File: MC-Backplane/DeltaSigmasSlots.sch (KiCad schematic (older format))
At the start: 2 parts, among them J21 86094328314755V1LF, J22 86094328314755V1LF

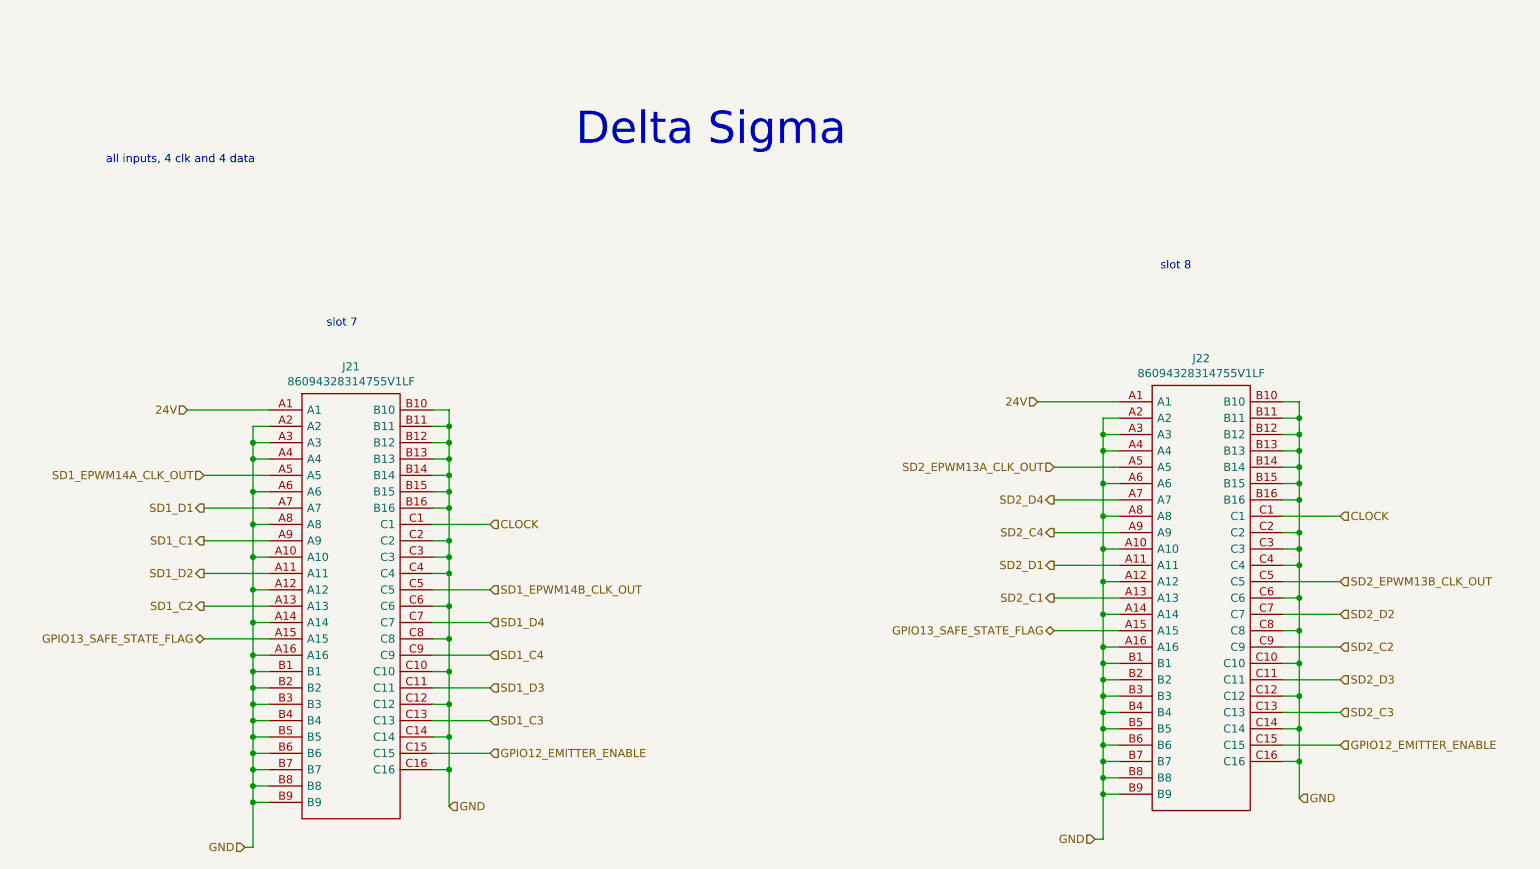
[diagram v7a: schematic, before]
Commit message: schematic reorg and layout begins
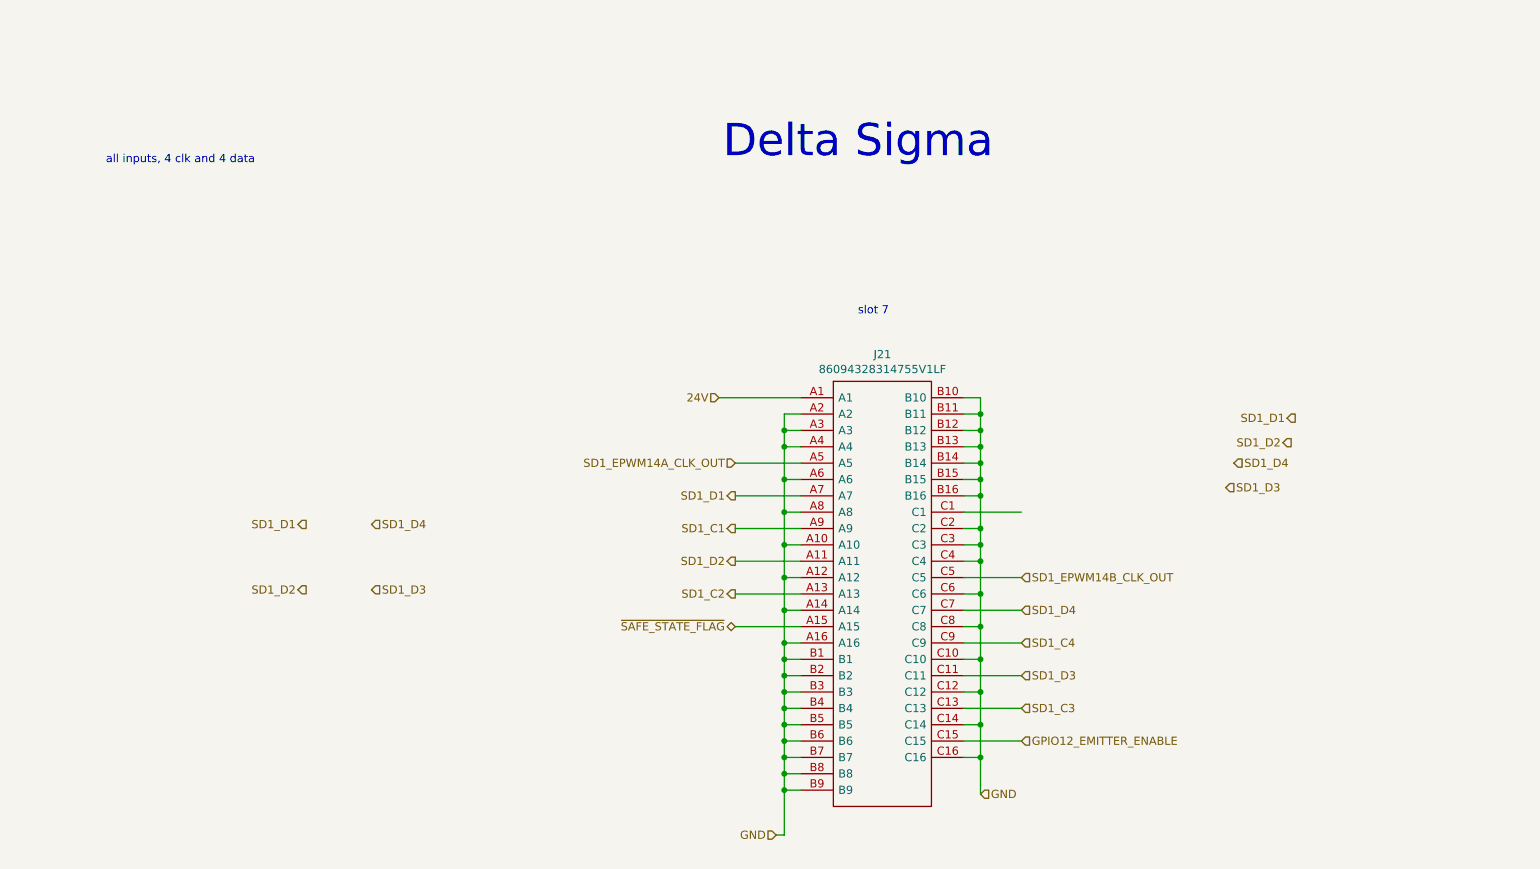
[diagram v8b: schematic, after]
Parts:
- removed J22: 86094328314755V1LF, 86094328314755V1LF, symbol Existing_IC_Models:86094328314755V1LF
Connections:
- net CLOCK: no longer names the net of J21.C1
- net GPIO13_SAFE_STATE_FLAG renamed ~SAFE_STATE_FLAG~
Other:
- note removed: "slot 8"
- moved on the sheet: J21
